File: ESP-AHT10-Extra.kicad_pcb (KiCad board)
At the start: 2 copper layers, 38.2 x 20.8 mm, 29 parts, among them J1 USB, SW1 RESET, SW2 PROG, U1 CH330N, U2 HT7233, U3 ESP-12, U4 AHT10, U5 USBLC6-2SC6

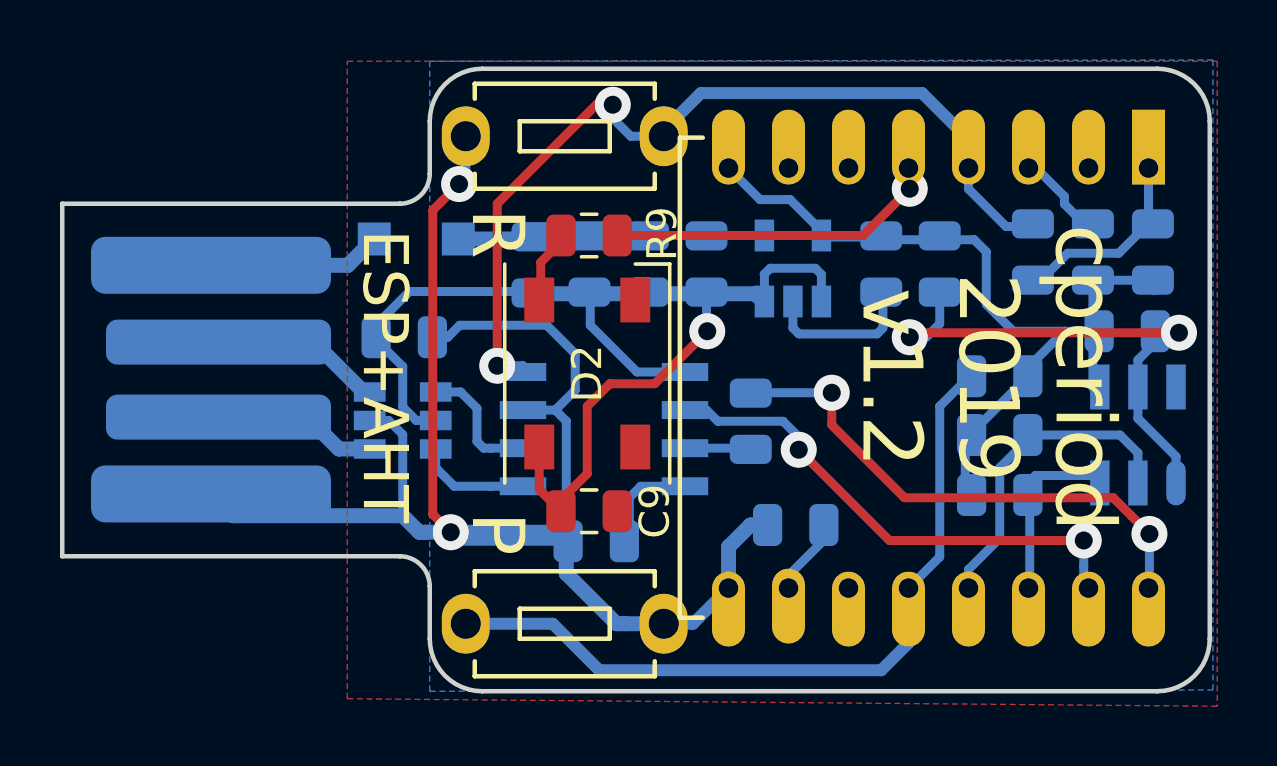
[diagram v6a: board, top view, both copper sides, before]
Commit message: drop the nightlight concept; it's not going to work with the power dissipation of a WLED. Clean things up for double-sided milling a bit more.
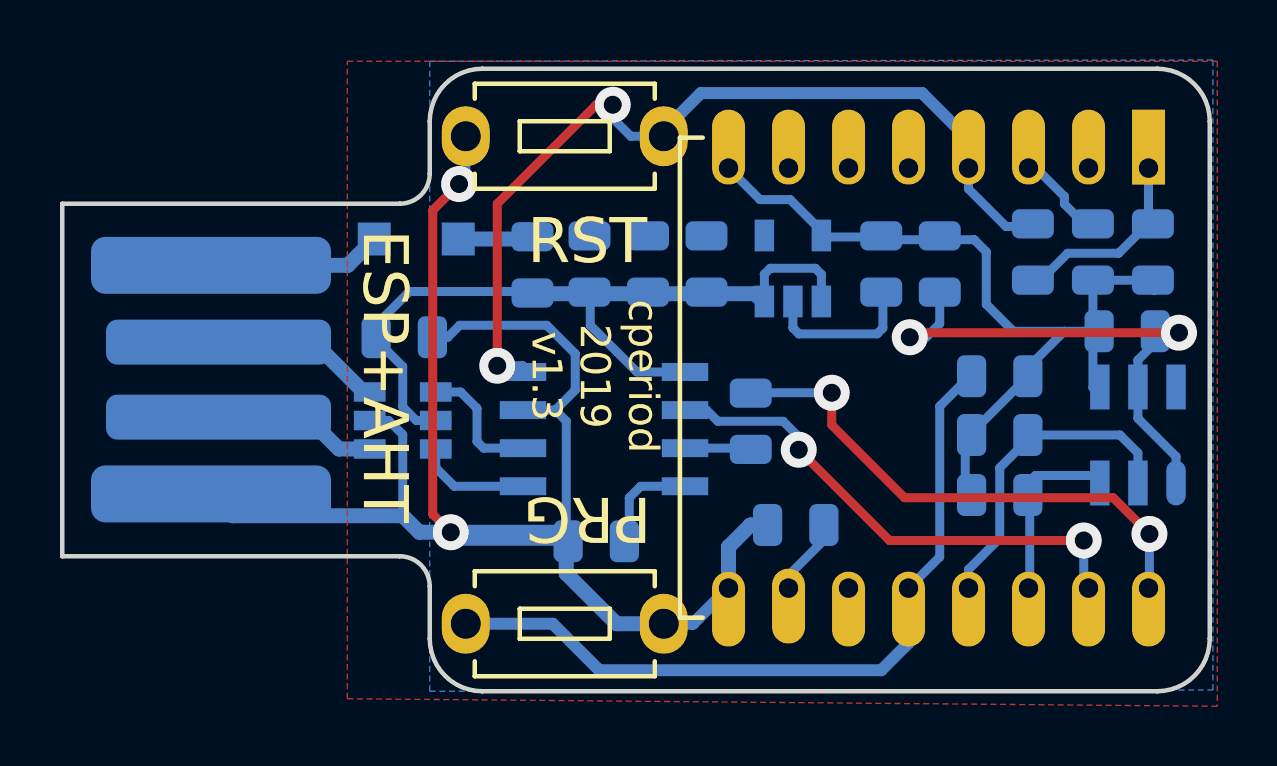
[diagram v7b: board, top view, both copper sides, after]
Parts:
- removed C9: 47u, Capacitor_SMD:C_0805_2012Metric
- removed D2: SK6812, LED_SMD:LED_SK6812_PLCC4_5.0x5.0mm_P3.2mm
- removed R9: 470R, Resistor_SMD:R_0805_2012Metric
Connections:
- U3 pad 5: WLED -> (no net)
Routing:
- net 5V: track 39.7 -> 27.0 mm, vias 1 -> 0
- net WLED: track 11.1 -> 0.00 mm, vias 1 -> 0
- net Net-(D2-Pad2): track 2.45 -> 0.00 mm
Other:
- board text added: "PRG"
- board text added: "RST"
- board text added: "cperiod 2019 v1.3"
- board text removed: "P"
- board text removed: "R"
- board text removed: "cperiod 2019 v1.2"

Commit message: minor silk tweaks
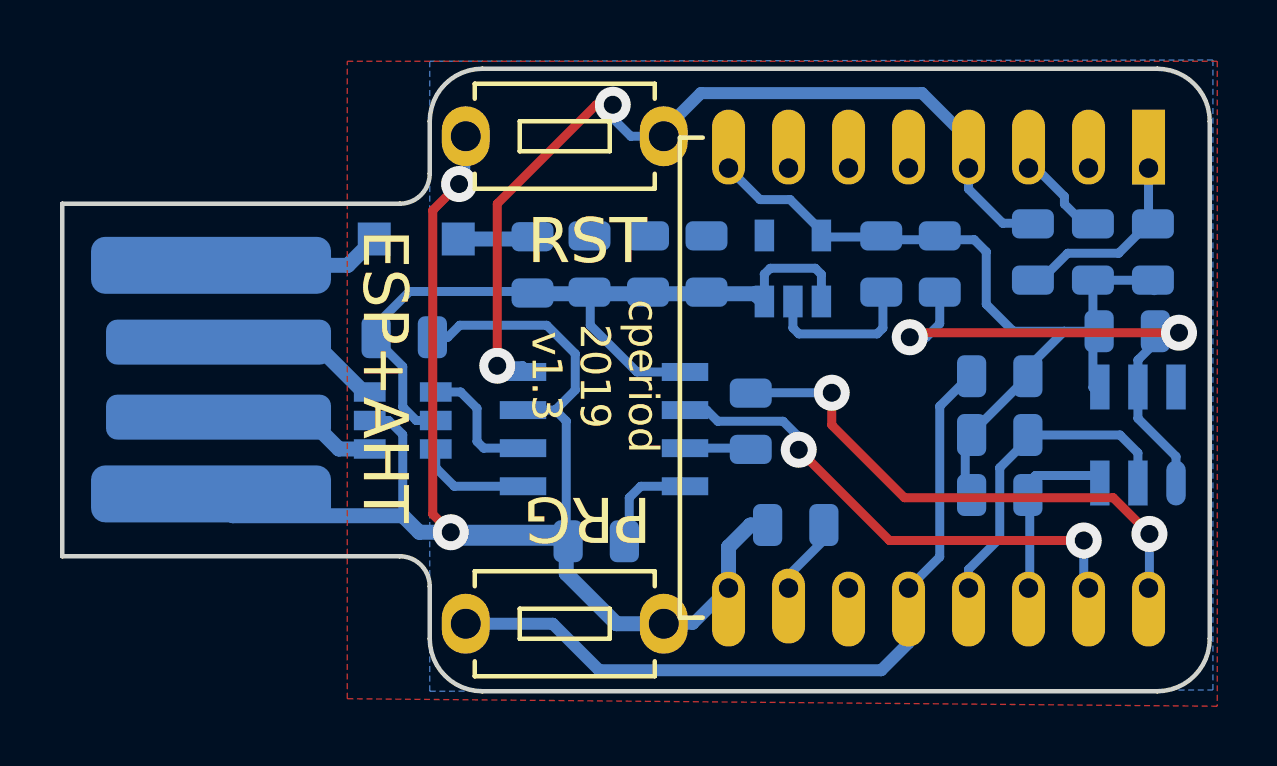
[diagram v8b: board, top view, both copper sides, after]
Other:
- board text added: "5V"
- board text added: "GND"
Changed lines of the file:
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@@
   (general
     (thickness 1.6)
-    (drawings 22)
-    (tracks 202)
+    (drawings 24)
+    (tracks 200)
     (zones 0)
     (modules 26)
@@
   )
   (layers
-    (0 F.Cu signal)
+    (0 F.Cu signal hide)
     (31 B.Cu signal)
-    (32 B.Adhes user)
-    (33 F.Adhes user)
+    (32 B.Adhes user hide)
+    (33 F.Adhes user hide)
     (34 B.Paste user)
-    (35 F.Paste user)
+    (35 F.Paste user hide)
     (36 B.SilkS user)
-    (37 F.SilkS user)
+    (37 F.SilkS user hide)
     (38 B.Mask user)
-    (39 F.Mask user)
-    (40 Dwgs.User user)
-    (41 Cmts.User user)
-    (42 Eco1.User user)
-    (43 Eco2.User user)
+    (39 F.Mask user hide)
+    (40 Dwgs.User user hide)
+    (41 Cmts.User user hide)
+    (42 Eco1.User user hide)
+    (43 Eco2.User user hide)
     (44 Edge.Cuts user)
-    (45 Margin user)
+    (45 Margin user hide)
     (46 B.CrtYd user)
-    (47 F.CrtYd user)
+    (47 F.CrtYd user hide)
     (48 B.Fab user)
-    (49 F.Fab user)
+    (49 F.Fab user hide)
   )
   (setup
@@
   (module CPB:AHT10-HandSolder locked (layer B.Cu)
     (at 165.855703 99.20862 90)
-    (fp_text reference U4 (at -2.79138 1.394297 180) (layer B.SilkS)
+    (fp_text reference U4 (at -2.99138 1.394297 180) (layer B.SilkS)
       (effects (font (size 1 1) (thickness 0.15)) (justify mirror))
     )
@@
     (tags SOT-23-6)
     (attr smd)
-    (fp_text reference U5 (at 0.05 2.525) (layer B.SilkS)
+    (fp_text reference U5 (at 1.15 2.525) (layer B.SilkS)
       (effects (font (size 1 1) (thickness 0.15)) (justify mirror))
     )
@@
     (tags capacitor)
     (attr smd)
-    (fp_text reference C5 (at -2.25 0) (layer B.SilkS)
+    (fp_text reference C5 (at -2.5 0) (layer B.SilkS)
       (effects (font (size 1 1) (thickness 0.15)) (justify mirror))
     )
@@
     (tags capacitor)
     (attr smd)
-    (fp_text reference C6 (at 2.3 0 180) (layer B.SilkS)
+    (fp_text reference C6 (at 2.55 0 180) (layer B.SilkS)
       (effects (font (size 1 1) (thickness 0.15)) (justify mirror))
     )
@@
       (effects (font (size 1 1) (thickness 0.15)) (justify mirror))
     )
-    (fp_text user %R (at -2.2 -0.075 180) (layer B.Fab)
+    (fp_text user %R (at 0.05 -1.575 180) (layer B.Fab) hide
       (effects (font (size 1 1) (thickness 0.15)) (justify mirror))
     )
@@
     (tags resistor)
     (attr smd)
-    (fp_text reference R1 (at 2.05862 -0.105703 180) (layer B.SilkS)
-      (effects (font (size 1 1) (thickness 0.15)) (justify mirror))
+    (fp_text reference R1 (at 1.85862 -0.055703 180) (layer B.SilkS)
+      (effects (font (size 0.8 0.8) (thickness 0.15)) (justify mirror))
     )
     (fp_text value 10K (at 8.05862 0.144297 90) (layer B.Fab)
@@
     (tags resistor)
     (attr smd)
-    (fp_text reference R2 (at 2.05862 -0.105703 180) (layer B.SilkS)
-      (effects (font (size 1 1) (thickness 0.15)) (justify mirror))
+    (fp_text reference R2 (at 1.85862 0.044297 180) (layer B.SilkS)
+      (effects (font (size 0.8 0.8) (thickness 0.15)) (justify mirror))
     )
     (fp_text value 1K (at 7.80862 0.144297 90) (layer B.Fab)
@@
     (tags resistor)
     (attr smd)
-    (fp_text reference R3 (at 2.05862 0.144297 180) (layer B.SilkS)
-      (effects (font (size 1 1) (thickness 0.15)) (justify mirror))
+    (fp_text reference R3 (at 1.85862 1.144297) (layer B.SilkS)
+      (effects (font (size 0.8 0.8) (thickness 0.15)) (justify mirror))
     )
     (fp_text value 10K (at 8.30862 -0.105703 90) (layer B.Fab)
@@
     (tags resistor)
     (attr smd)
-    (fp_text reference R4 (at -2.3 -0.04138 180) (layer B.SilkS)
+    (fp_text reference R4 (at -2.45 -0.04138 180) (layer B.SilkS)
       (effects (font (size 1 1) (thickness 0.15)) (justify mirror))
     )
@@
     (tags resistor)
     (attr smd)
-    (fp_text reference R5 (at 2.25 0 180) (layer B.SilkS)
+    (fp_text reference R5 (at 2.5 0 180) (layer B.SilkS)
       (effects (font (size 1 1) (thickness 0.15)) (justify mirror))
     )
@@
     (tags resistor)
     (attr smd)
-    (fp_text reference R6 (at -2.25 0.04138) (layer B.SilkS)
+    (fp_text reference R6 (at -2.5 0.04138) (layer B.SilkS)
       (effects (font (size 1 1) (thickness 0.15)) (justify mirror))
     )
@@
     (tags resistor)
     (attr smd)
-    (fp_text reference R7 (at -2.25 0.04138) (layer B.SilkS)
+    (fp_text reference R7 (at -2.5 0.04138) (layer B.SilkS)
       (effects (font (size 1 1) (thickness 0.15)) (justify mirror))
     )
@@
     )
   )
+  (gr_text GND (at 140.25 102.5) (layer B.SilkS)
+    (effects (font (size 1 1) (thickness 0.25)) (justify mirror))
+  )
+  (gr_text 5V (at 140 94.25) (layer B.SilkS)
+    (effects (font (size 1 1) (thickness 0.25)) (justify mirror))
+  )
   (gr_text "cperiod\n2019\nv1.3" (at 147.75 97.25 270) (layer F.SilkS)
     (effects (font (size 1 1) (thickness 0.2)))
   )
   (gr_text "cperiod\n2019\nv1.3" (at 147.75 97.25 270) (layer F.Cu)
-    (effects (font (size 1 1) (thickness 0.2)))
+    (effects (font (size 1 1) (thickness 0.15)))
   )
   (gr_text PRG (at 147.5 102 180) (layer F.SilkS)
@@
   (segment (start 164.355703 97.62862) (end 164.585703 97.85862) (width 0.3) (layer B.Cu) (net 1) (status 30))
   (segment (start 164.355703 94.055703) (end 164.355703 97.62862) (width 0.3) (layer B.Cu) (net 1) (status 30))
-  (segment (start 164.35 94.05) (end 164.355703 94.055703) (width 0.3) (layer B.Cu) (net 1) (status 30))
   (segment (start 166.4 94.4) (end 166.05 94.05) (width 0.3) (layer B.Cu) (net 1) (status 30))
   (segment (start 166.05 94.05) (end 164.35 94.05) (width 0.3) (layer B.Cu) (net 1) (status 30))
@@
   (segment (start 145.7 94.55) (end 145.75 94.5) (width 0.5) (layer B.Cu) (net 17) (status 30))
   (segment (start 145.75 94.5) (end 153.097083 94.5) (width 0.5) (layer B.Cu) (net 17) (status 30))
+  (segment (start 150.759217 99.647374) (end 152.897374 99.647374) (width 0.3) (layer B.Cu) (net 18) (status 30))
   (segment (start 152.897374 99.647374) (end 152.925 99.675) (width 0.3) (layer B.Cu) (net 18) (status 30))
-  (segment (start 150.759217 99.647374) (end 152.897374 99.647374) (width 0.3) (layer B.Cu) (net 18) (status 30))
   (segment (start 145.525 92.675) (end 145.675 92.825) (width 0.5) (layer B.Cu) (net 19) (status 30))
   (segment (start 143.2 92.675) (end 145.525 92.675) (width 0.5) (layer B.Cu) (net 19) (status 30))
@@
   (segment (start 144.5 96.9) (end 144.5 91.5) (width 0.3) (layer F.Cu) (net 20))
   (segment (start 144.5 91.5) (end 147.8 88.2) (width 0.3) (layer F.Cu) (net 20))
-  (segment (start 160.209217 91.009217) (end 160.209217 90.312374) (width 0.3) (layer B.Cu) (net 20) (status 20))
-  (segment (start 162.355703 92.25862) (end 161.45862 92.25862) (width 0.3) (layer B.Cu) (net 20) (status 10))
-  (segment (start 161.45862 92.25862) (end 160.209217 91.009217) (width 0.3) (layer B.Cu) (net 20))
-  (segment (start 158.209217 90.312374) (end 158.187626 90.312374) (width 0.3) (layer F.Cu) (net 0) (status 30))
+  (segment (start 162.3 92.15) (end 161.35 92.15) (width 0.3) (layer B.Cu) (net 20))
+  (segment (start 160.209217 91.009217) (end 160.209217 90.312374) (width 0.3) (layer B.Cu) (net 20))
+  (segment (start 161.35 92.15) (end 160.209217 91.009217) (width 0.3) (layer B.Cu) (net 20))
   (zone (net 0) (net_name "") (layers F&B.Cu) (hatch edge 0.508)
     (connect_pads (clearance 0.508))
